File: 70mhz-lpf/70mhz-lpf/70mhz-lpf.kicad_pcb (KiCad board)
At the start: 2 copper layers, 78.7 x 38.1 mm, 15 parts, among them J701 Coax Solder Point, J702 Coax Solder Point

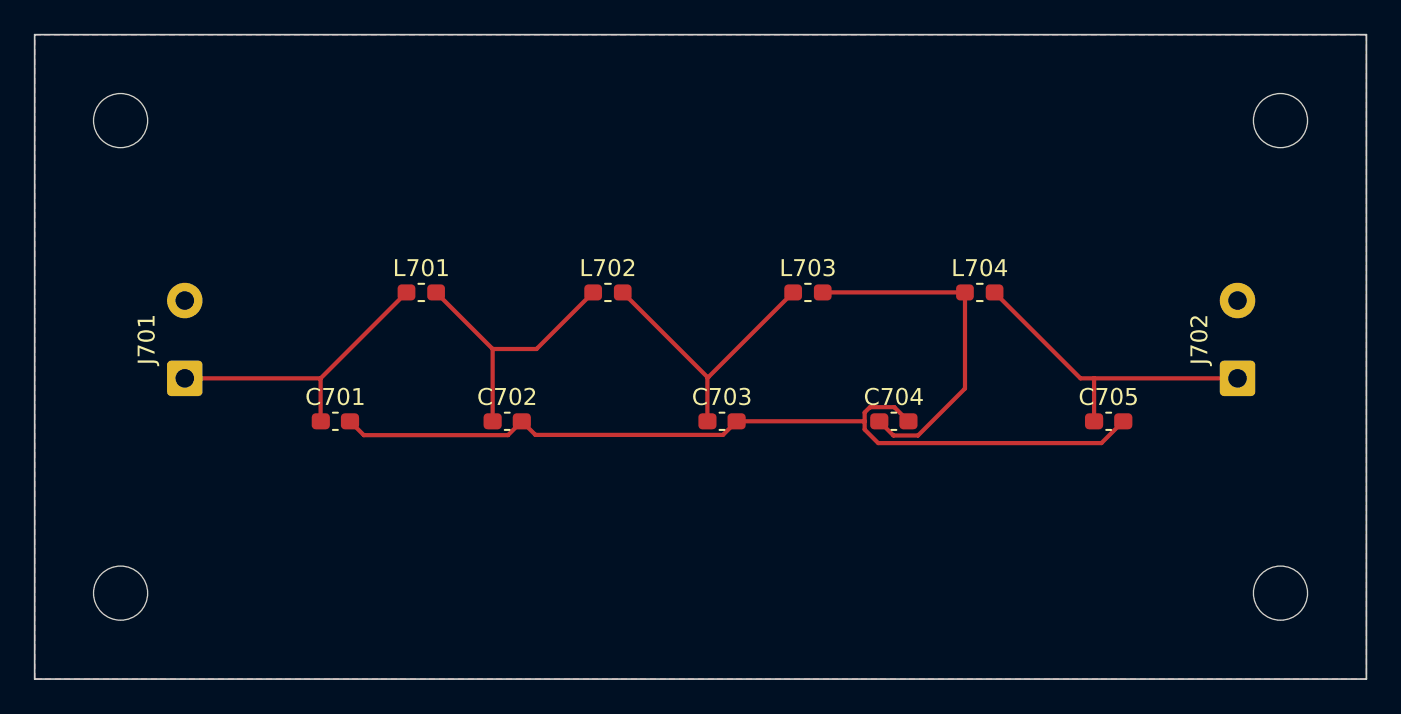
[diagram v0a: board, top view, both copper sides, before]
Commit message: Hierarchical schematic updates
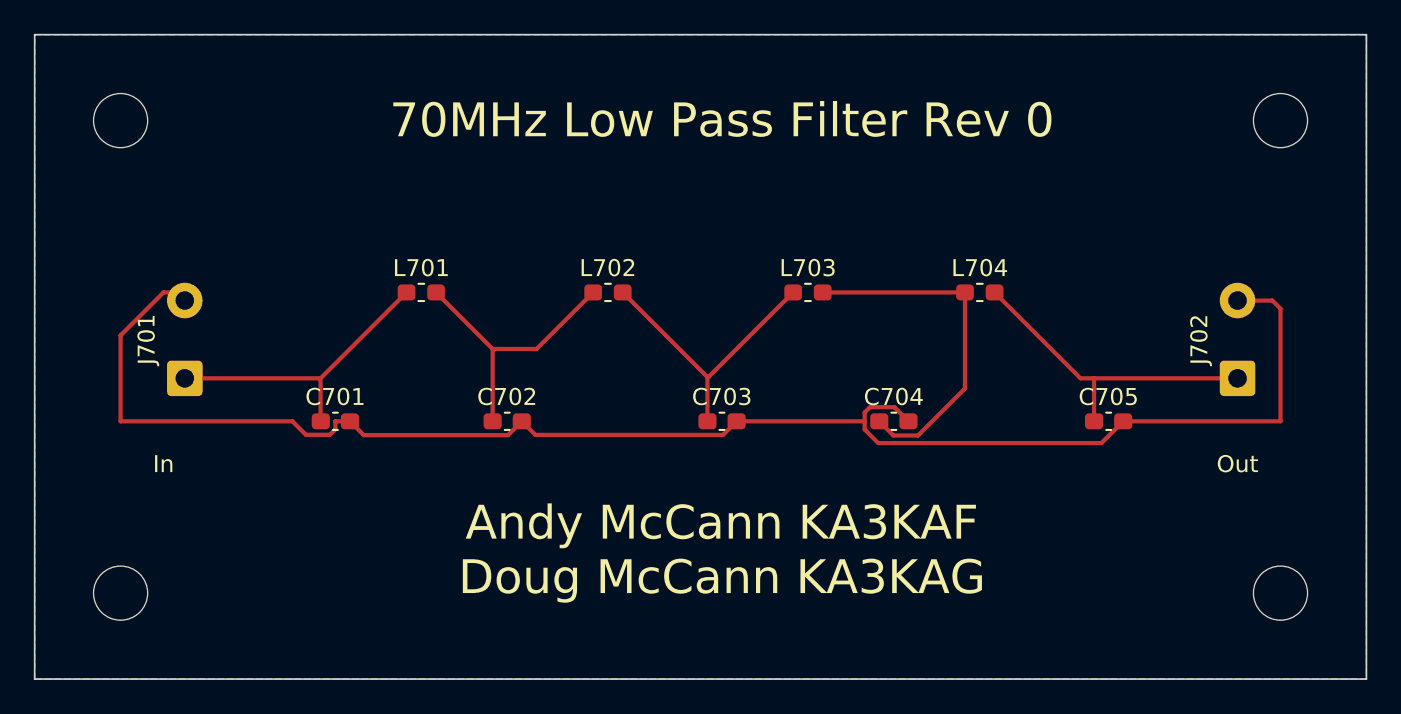
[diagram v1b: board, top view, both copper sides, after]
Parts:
- turned H703 to 90 degrees
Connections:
- J701 pad 2: unconnected-(J701-Pad2) -> GND
- J702 pad 2: unconnected-(J702-Pad2) -> GND
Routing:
- net GND: track 52.0 -> 95.3 mm
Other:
- board text added: "70MHz Low Pass Filter Rev 0"
- board text added: "Andy McCann KA3KAF Doug McCann KA3KAG"
- board text added: "In"
- board text added: "Out"
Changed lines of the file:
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@@
   )
   (setup
+    (stackup
+      (layer "F.SilkS" (type "Top Silk Screen"))
+      (layer "F.Paste" (type "Top Solder Paste"))
+      (layer "F.Mask" (type "Top Solder Mask") (thickness 0.01))
+      (layer "F.Cu" (type "copper") (thickness 0.035))
+      (layer "dielectric 1" (type "core") (thickness 1.51) (material "FR4") (epsilon_r 4.5) (loss_tangent 0.02))
+      (layer "B.Cu" (type "copper") (thickness 0.035))
+      (layer "B.Mask" (type "Bottom Solder Mask") (thickness 0.01))
+      (layer "B.Paste" (type "Bottom Solder Paste"))
+      (layer "B.SilkS" (type "Bottom Silk Screen"))
+      (copper_finish "None")
+      (dielectric_constraints no)
+    )
     (pad_to_mask_clearance 0)
     (grid_origin 114.3 111.76)
@@
   (net 5 "Net-(C704-Pad1)")
   (net 6 "Net-(C705-Pad1)")
-  (net 7 "unconnected-(J701-Pad2)")
-  (net 8 "unconnected-(J702-Pad2)")
   (footprint "Capacitor_SMD:C_0603_1608Metric_Pad1.08x0.95mm_HandSolder" (layer "F.Cu")
     (at 165.1 96.52)
@@
       (effects (font (size 1 1) (thickness 0.15)))
     )
-    (fp_text value "Coax Solder Point" (at 2.3 2.25 90) (layer "F.Fab")
+    (fp_text value "Coax Solder Point" (at 2.3 2.25 90) (layer "F.Fab") hide
       (effects (font (size 1 1) (thickness 0.15)))
     )
@@
       (net 1 "Net-(C701-Pad1)") (pinfunction "In") (pintype "passive"))
     (pad "2" thru_hole circle (at 4.6 0 90) (size 2.1 2.1) (drill 1.1) (layers *.Cu *.Mask)
-      (net 7 "unconnected-(J701-Pad2)") (pinfunction "Ext") (pintype "passive"))
+      (net 2 "GND") (pinfunction "Ext") (pintype "passive"))
     (model "${KICAD6_3DMODEL_DIR}/Connector_Wire.3dshapes/SolderWire-0.5sqmm_1x02_P4.6mm_D0.9mm_OD2.1mm.wrl"
       (offset (xyz 0 0 0))
@@
       (effects (font (size 1 1) (thickness 0.15)))
     )
-    (fp_text user "${REFERENCE}" (at 0 0) (layer "F.Fab")
+    (fp_text user "${REFERENCE}" (at 0 0) (layer "F.Fab") hide
       (effects (font (size 1 1) (thickness 0.15)))
     )
@@
       (effects (font (size 1 1) (thickness 0.15)))
     )
-    (fp_text user "${REFERENCE}" (at 0 0) (layer "F.Fab")
+    (fp_text user "${REFERENCE}" (at 0 0) (layer "F.Fab") hide
       (effects (font (size 1 1) (thickness 0.15)))
     )
@@
       (effects (font (size 1 1) (thickness 0.15)))
     )
-    (fp_text value "Coax Solder Point" (at 2.3 2.25 90) (layer "F.Fab")
+    (fp_text value "Coax Solder Point" (at 2.3 2.25 90) (layer "F.Fab") hide
       (effects (font (size 1 1) (thickness 0.15)))
     )
@@
       (net 6 "Net-(C705-Pad1)") (pinfunction "In") (pintype "passive"))
     (pad "2" thru_hole circle (at 4.6 0 90) (size 2.1 2.1) (drill 1.1) (layers *.Cu *.Mask)
-      (net 8 "unconnected-(J702-Pad2)") (pinfunction "Ext") (pintype "passive"))
+      (net 2 "GND") (pinfunction "Ext") (pintype "passive"))
     (model "${KICAD6_3DMODEL_DIR}/Connector_Wire.3dshapes/SolderWire-0.5sqmm_1x02_P4.6mm_D0.9mm_OD2.1mm.wrl"
       (offset (xyz 0 0 0))
@@
       (effects (font (size 1 1) (thickness 0.15)))
     )
-    (fp_text user "${REFERENCE}" (at 0 0) (layer "F.Fab")
+    (fp_text user "${REFERENCE}" (at 0 0) (layer "F.Fab") hide
       (effects (font (size 1 1) (thickness 0.15)))
     )
@@
   )
   (footprint "MountingHole:MountingHole_3.2mm_M3" (layer "F.Cu")
-    (at 187.96 78.74)
+    (at 187.96 78.74 90)
     (descr "Mounting Hole 3.2mm, no annular, M3")
     (tags "mounting hole 3.2mm no annular m3")
@@
     (property "Sheetname" "")
     (attr exclude_from_pos_files)
-    (fp_text reference "H703" (at 0 -4.2) (layer "F.SilkS") hide
-      (effects (font (size 1 1) (thickness 0.15)))
-    )
-    (fp_text value "MountingHole" (at 0 4.2) (layer "F.Fab") hide
-      (effects (font (size 1 1) (thickness 0.15)))
-    )
-    (fp_text user "${REFERENCE}" (at 0 0) (layer "F.Fab")
+    (fp_text reference "H703" (at 0 -4.2 90) (layer "F.SilkS") hide
+      (effects (font (size 1 1) (thickness 0.15)))
+    )
+    (fp_text value "MountingHole" (at 0 4.2 90) (layer "F.Fab") hide
+      (effects (font (size 1 1) (thickness 0.15)))
+    )
+    (fp_text user "${REFERENCE}" (at 0 0 90) (layer "F.Fab") hide
       (effects (font (size 1 1) (thickness 0.15)))
     )
     (fp_circle (center 0 0) (end 3.2 0) (layer "Cmts.User") (width 0.15) (fill none))
     (fp_circle (center 0 0) (end 3.45 0) (layer "F.CrtYd") (width 0.05) (fill none))
-    (pad "" np_thru_hole circle (at 0 0) (size 3.2 3.2) (drill 3.2) (layers *.Cu *.Mask))
+    (pad "" np_thru_hole circle (at 0 0 90) (size 3.2 3.2) (drill 3.2) (layers *.Cu *.Mask))
   )
   (footprint "Capacitor_SMD:C_0603_1608Metric_Pad1.08x0.95mm_HandSolder" (layer "F.Cu")
@@
   )
   (gr_rect (start 114.3 73.66) (end 193.04 111.76) (layer "Edge.Cuts") (width 0.1) (fill none))
+  (gr_text "Andy McCann KA3KAF\nDoug McCann KA3KAG" (at 154.94 104.14) (layer "F.SilkS")
+    (effects (font (size 2 2) (thickness 0.25)))
+  )
+  (gr_text "In" (at 121.92 99.06) (layer "F.SilkS")
+    (effects (font (size 1 1) (thickness 0.15)))
+  )
+  (gr_text "Out" (at 185.42 99.06) (layer "F.SilkS")
+    (effects (font (size 1 1) (thickness 0.15)))
+  )
+  (gr_text "70MHz Low Pass Filter Rev 0" (at 154.94 78.74) (layer "F.SilkS")
+    (effects (font (size 2 2) (thickness 0.25)))
+  )
   (segment (start 131.205 96.5075) (end 131.205 93.98) (width 0.25) (layer "F.Cu") (net 1))
   (segment (start 123.176 93.98) (end 131.205 93.98) (width 0.25) (layer "F.Cu") (net 1))
   (segment (start 131.205 93.98) (end 136.285 88.9) (width 0.25) (layer "F.Cu") (net 1))
   (segment (start 131.2175 96.52) (end 131.205 96.5075) (width 0.25) (layer "F.Cu") (net 1))
+  (segment (start 187.48 89.38) (end 187.96 89.86) (width 0.25) (layer "F.Cu") (net 2))
   (segment (start 163.3737 96.52) (end 155.8025 96.52) (width 0.25) (layer "F.Cu") (net 2))
   (segment (start 165.1286 95.6861) (end 165.9625 96.52) (width 0.25) (layer "F.Cu") (net 2))
+  (segment (start 119.38 91.44) (end 119.38 96.52) (width 0.25) (layer "F.Cu") (net 2))
+  (segment (start 185.42 89.38) (end 187.48 89.38) (width 0.25) (layer "F.Cu") (net 2))
+  (segment (start 132.08 96.990495) (end 132.08 96.52) (width 0.25) (layer "F.Cu") (net 2))
   (segment (start 132.9425 96.52) (end 133.762 97.3395) (width 0.25) (layer "F.Cu") (net 2))
   (segment (start 142.283 97.3395) (end 143.1025 96.52) (width 0.25) (layer "F.Cu") (net 2))
   (segment (start 133.762 97.3395) (end 142.283 97.3395) (width 0.25) (layer "F.Cu") (net 2))
+  (segment (start 123.176 89.38) (end 122.696 88.9) (width 0.25) (layer "F.Cu") (net 2))
+  (segment (start 119.38 96.52) (end 129.54 96.52) (width 0.25) (layer "F.Cu") (net 2))
   (segment (start 164.1778 97.8086) (end 163.3737 97.0045) (width 0.25) (layer "F.Cu") (net 2))
+  (segment (start 132.08 96.52) (end 132.9425 96.52) (width 0.25) (layer "F.Cu") (net 2))
+  (segment (start 187.96 89.86) (end 187.96 96.52) (width 0.25) (layer "F.Cu") (net 2))
+  (segment (start 122.696 88.9) (end 121.92 88.9) (width 0.25) (layer "F.Cu") (net 2))
   (segment (start 163.3737 97.0045) (end 163.3737 96.52) (width 0.25) (layer "F.Cu") (net 2))
   (segment (start 163.6864 95.6861) (end 165.1286 95.6861) (width 0.25) (layer "F.Cu") (net 2))
   (segment (start 143.9059 97.3234) (end 154.9991 97.3234) (width 0.25) (layer "F.Cu") (net 2))
+  (segment (start 121.92 88.9) (end 119.38 91.44) (width 0.25) (layer "F.Cu") (net 2))
   (segment (start 177.3739 97.8086) (end 164.1778 97.8086) (width 0.25) (layer "F.Cu") (net 2))
   (segment (start 178.6625 96.52) (end 177.3739 97.8086) (width 0.25) (layer "F.Cu") (net 2))
+  (segment (start 131.750495 97.32) (end 132.08 96.990495) (width 0.25) (layer "F.Cu") (net 2))
   (segment (start 163.3737 95.9988) (end 163.6864 95.6861) (width 0.25) (layer "F.Cu") (net 2))
   (segment (start 143.1025 96.52) (end 143.9059 97.3234) (width 0.25) (layer "F.Cu") (net 2))
+  (segment (start 129.54 96.52) (end 130.34 97.32) (width 0.25) (layer "F.Cu") (net 2))
   (segment (start 163.3737 96.52) (end 163.3737 95.9988) (width 0.25) (layer "F.Cu") (net 2))
   (segment (start 154.9991 97.3234) (end 155.8025 96.52) (width 0.25) (layer "F.Cu") (net 2))
+  (segment (start 187.96 96.52) (end 178.6625 96.52) (width 0.25) (layer "F.Cu") (net 2))
+  (segment (start 130.34 97.32) (end 131.750495 97.32) (width 0.25) (layer "F.Cu") (net 2))
   (segment (start 141.3775 92.2425) (end 143.9775 92.2425) (width 0.25) (layer "F.Cu") (net 3))
   (segment (start 141.3775 92.2425) (end 138.035 88.9) (width 0.25) (layer "F.Cu") (net 3))

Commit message: minor changes to 5 boards
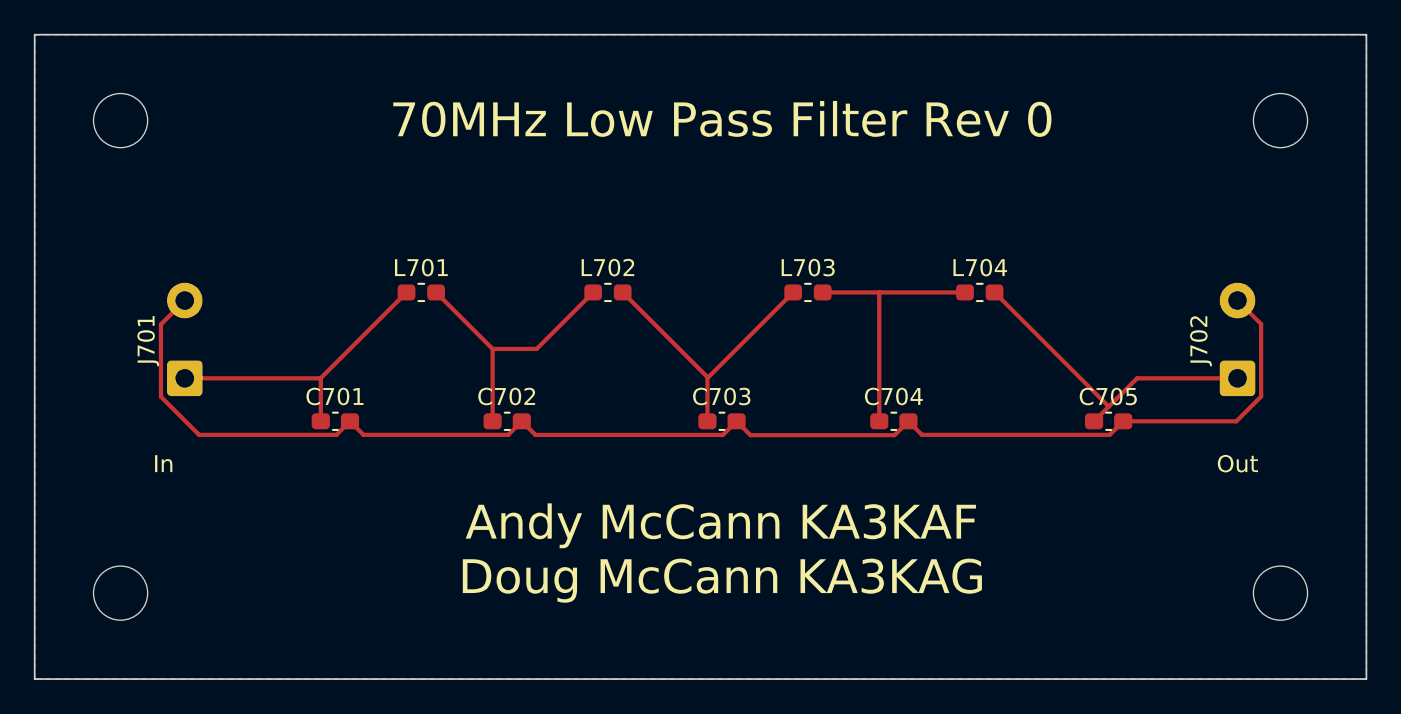
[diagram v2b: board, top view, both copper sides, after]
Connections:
- net Net-(C701-Pad1) renamed /In
- net Net-(C705-Pad1) renamed /Out
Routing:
- net GND: track 95.3 -> 82.1 mm
- net Net-(C704-Pad1): track 20.7 -> 16.0 mm

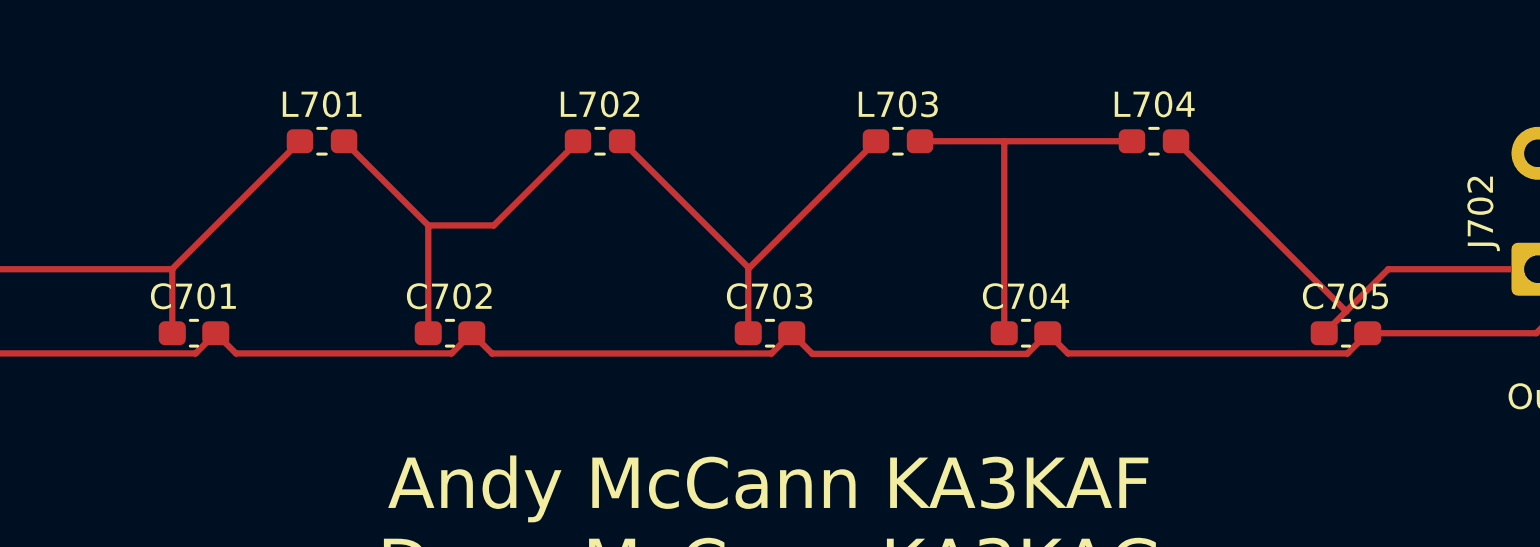
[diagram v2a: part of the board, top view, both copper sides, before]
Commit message: Fixes to 2ndmixer-2ndlo and vco-1stmixer
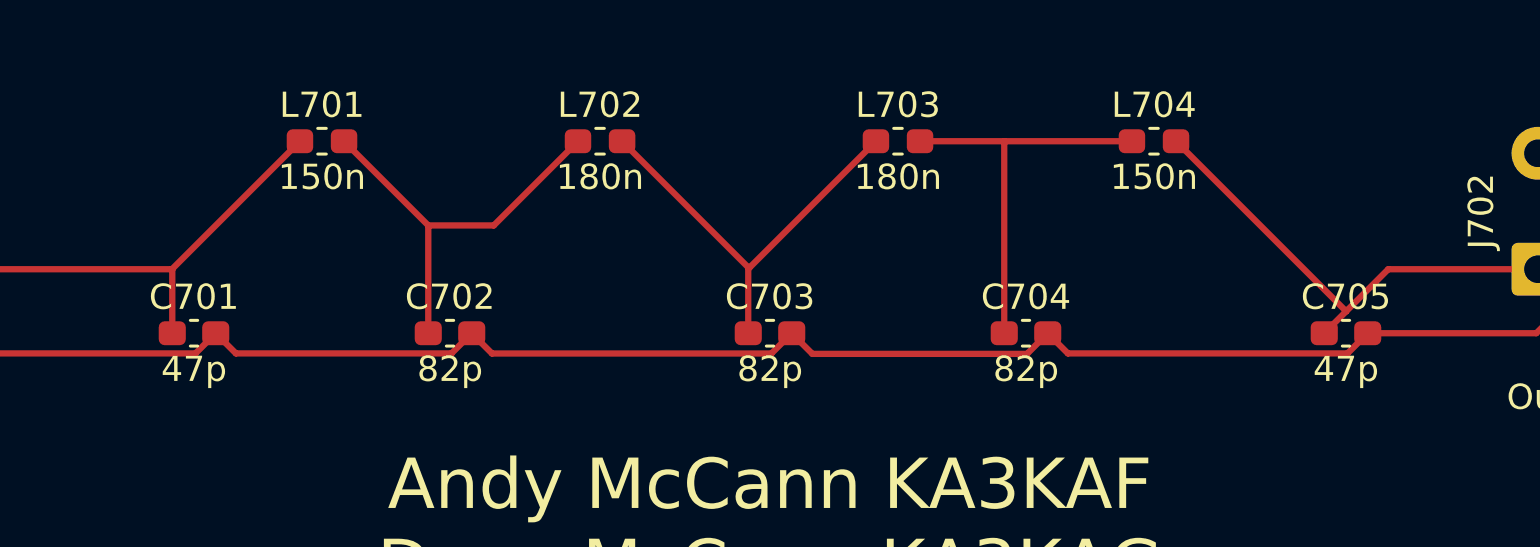
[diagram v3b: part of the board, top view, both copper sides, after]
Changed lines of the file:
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@@
       (effects (font (size 1 1) (thickness 0.15)))
     )
-    (fp_text value "82p" (at 0 1.43) (layer "F.Fab")
+    (fp_text value "82p" (at 0 1.43) (layer "F.SilkS")
       (effects (font (size 1 1) (thickness 0.15)))
     )
@@
       (effects (font (size 1 1) (thickness 0.15)))
     )
-    (fp_text value "180n" (at 0 1.43) (layer "F.Fab")
+    (fp_text value "180n" (at 0 1.43) (layer "F.SilkS")
       (effects (font (size 1 1) (thickness 0.15)))
     )
@@
       (effects (font (size 1 1) (thickness 0.15)))
     )
-    (fp_text value "180n" (at 0 1.43) (layer "F.Fab")
+    (fp_text value "180n" (at 0 1.43) (layer "F.SilkS")
       (effects (font (size 1 1) (thickness 0.15)))
     )
@@
       (effects (font (size 1 1) (thickness 0.15)))
     )
-    (fp_text value "47p" (at 0 1.43) (layer "F.Fab")
+    (fp_text value "47p" (at 0 1.43) (layer "F.SilkS")
       (effects (font (size 1 1) (thickness 0.15)))
     )
@@
       (effects (font (size 1 1) (thickness 0.15)))
     )
-    (fp_text value "47p" (at 0 1.43) (layer "F.Fab")
+    (fp_text value "47p" (at 0 1.43) (layer "F.SilkS")
       (effects (font (size 1 1) (thickness 0.15)))
     )
@@
       (effects (font (size 1 1) (thickness 0.15)))
     )
-    (fp_text value "150n" (at 0 1.43) (layer "F.Fab")
+    (fp_text value "150n" (at 0 1.43) (layer "F.SilkS")
       (effects (font (size 1 1) (thickness 0.15)))
     )
@@
       (effects (font (size 1 1) (thickness 0.15)))
     )
-    (fp_text value "150n" (at 0 1.43) (layer "F.Fab")
+    (fp_text value "150n" (at 0 1.43) (layer "F.SilkS")
       (effects (font (size 1 1) (thickness 0.15)))
     )
@@
       (effects (font (size 1 1) (thickness 0.15)))
     )
-    (fp_text value "82p" (at 0 1.43) (layer "F.Fab")
+    (fp_text value "82p" (at 0 1.43) (layer "F.SilkS")
       (effects (font (size 1 1) (thickness 0.15)))
     )
@@
       (effects (font (size 1 1) (thickness 0.15)))
     )
-    (fp_text value "82p" (at 0 1.43) (layer "F.Fab")
-      (effects (font (size 1 1) (thickness 0.15)))
-    )
+    (fp_text value "82p" (at 0 1.43) (layer "F.SilkS")
+      (effects (font (size 1 1) (thickness 0.15)))
+    )
